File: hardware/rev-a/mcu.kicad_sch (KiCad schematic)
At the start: 6 parts, among them J1 Conn_01x05, SW1 SW_Push, U3 MDBT42Q-512K

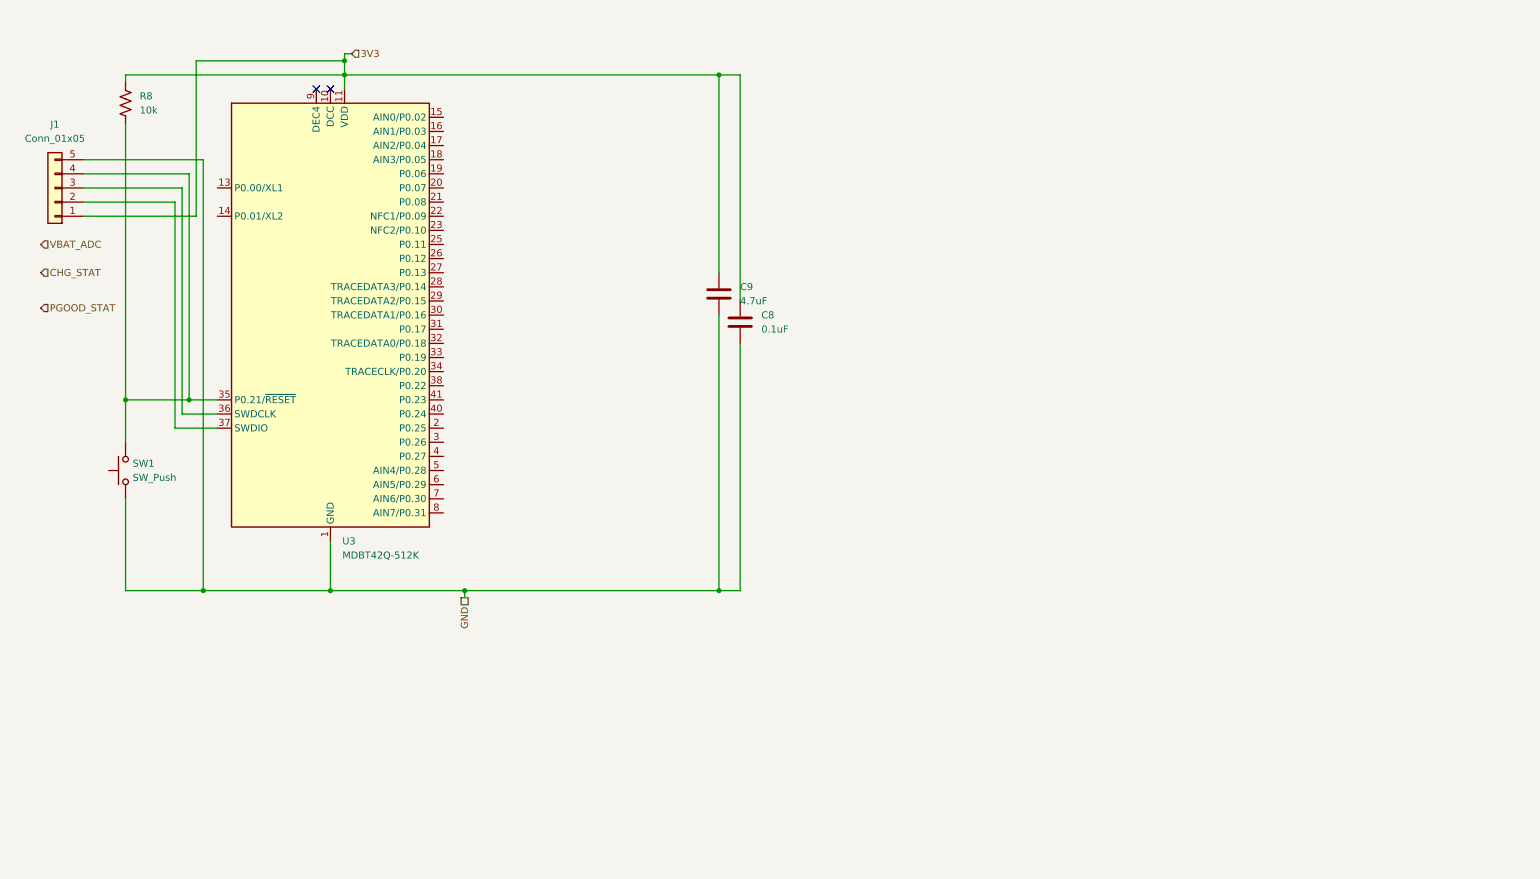
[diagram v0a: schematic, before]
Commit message: finalize MCU sheet and add haptic feedback sheet
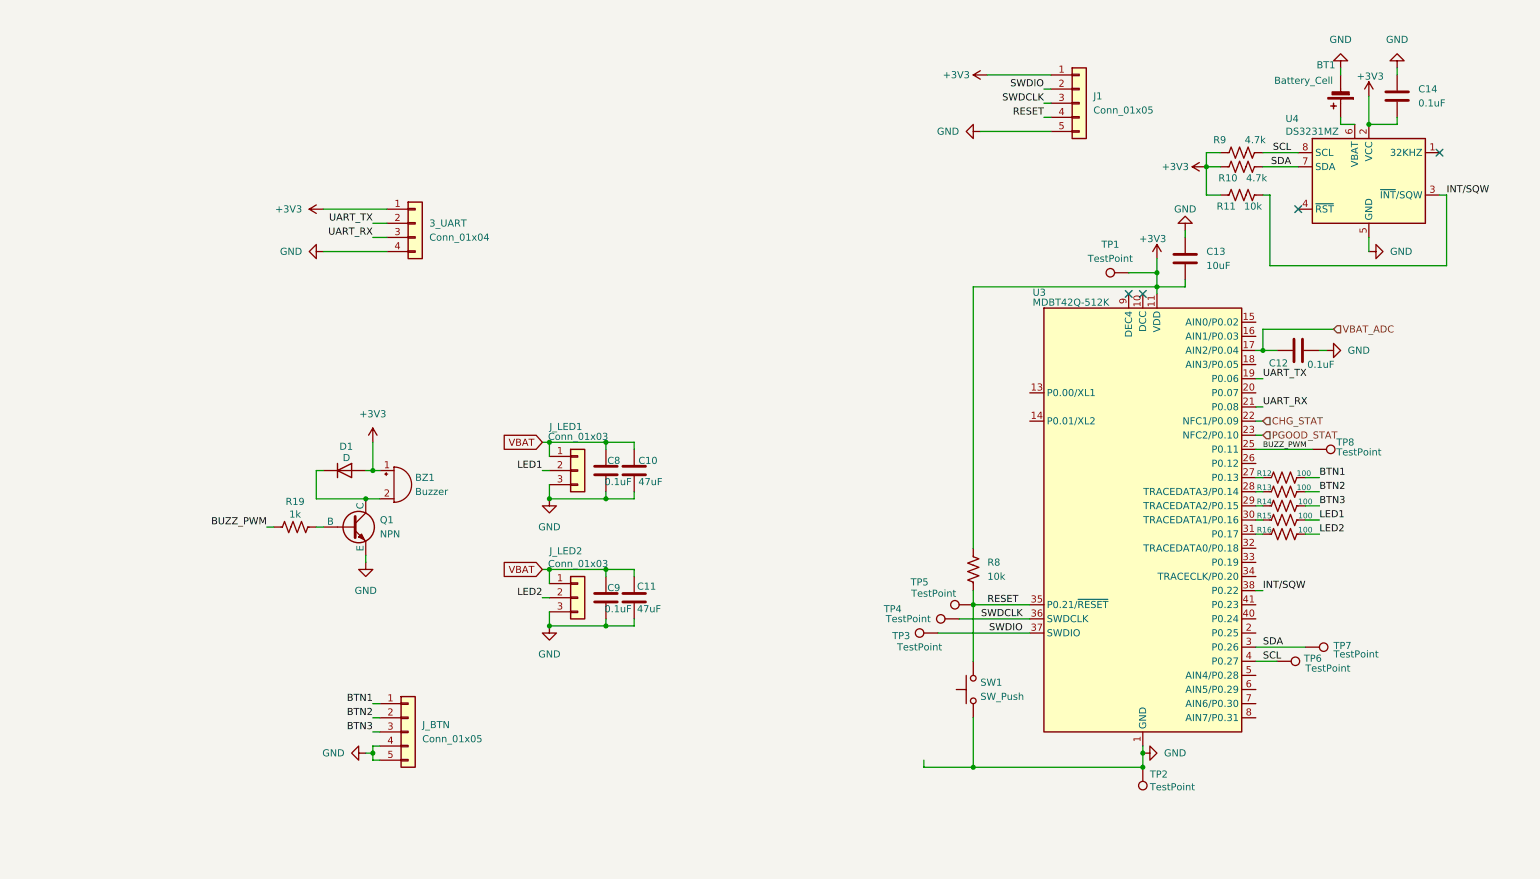
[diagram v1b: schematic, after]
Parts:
- added 3_UART: Conn_01x04, symbol Connector_Generic:Conn_01x04
- added BT1: Battery_Cell, symbol Device:Battery_Cell
- added BZ1: Buzzer, symbol Device:Buzzer
- added C10, C11: 47uF, symbol Device:C
- added C12, C14: 0.1uF, symbol Device:C
- added C13: 10uF, symbol Device:C
- added D1: D, symbol Device:D
- added J_BTN: Conn_01x05, symbol Connector_Generic:Conn_01x05
- added J_LED1, J_LED2: Conn_01x03, symbol Connector_Generic:Conn_01x03
- added Q1: NPN, symbol Simulation_SPICE:NPN
- added R10, R9: 4.7k, symbol Device:R_US
- added R11: 10k, symbol Device:R_US
- added R12, R13, R14, R15, R16: 100, symbol Device:R_US
- added R19: 1k, symbol Device:R_US
- added TP1, TP2, TP3, TP4, TP5, TP6, TP7, TP8: TestPoint, symbol Connector:TestPoint
- added U4: DS3231MZ, Package_SO:SOIC-8_3.9x4.9mm_P1.27mm, symbol Timer_RTC:DS3231MZ
- C9: value 4.7uF -> 0.1uF
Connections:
- net CHG_STAT: now also U3.22 (NFC1/P0.09)
- net GND: now also 3_UART.4 (Pin_4), BT1.2 (-), C10.2, C11.2, C12.2, C13.1, C14.1, J_BTN.4 (Pin_4), J_BTN.5 (Pin_5), J_LED1.3 (Pin_3), J_LED2.3 (Pin_3), Q1.3 (E), TP2.1, U4.5 (GND)
- net PGOOD_STAT: now also U3.23 (NFC2/P0.10)
- net VBAT_ADC: now also U3.17 (AIN2/P0.04), C12.1
- net UART_TX: now reaches U3.19 (P0.06)
- net UART_TX: now also 3_UART.2 (Pin_2)
- net UART_RX: now reaches U3.21 (P0.08)
- net UART_RX: now also 3_UART.3 (Pin_3)
- net BUZZ_PWM: now reaches U3.25 (P0.11)
- net BUZZ_PWM: now also R19.1, TP8.1
- net at U3.27 (P0.13): now also R12.1
- net at U3.28 (TRACEDATA3/P0.14): now also R13.1
- net at U3.29 (TRACEDATA2/P0.15): now also R14.1
- net SDA: now reaches U3.3 (P0.26)
- net SDA: now also R10.2, TP7.1, U4.7 (SDA)
- net at U3.30 (TRACEDATA1/P0.16): now also R15.2
- net at U3.31 (P0.17): now also R16.2
- net RESET: now reaches J1.4 (Pin_4), R8.2, SW1.2, U3.35 (P0.21/~{RESET})
- net RESET: now also TP5.1
- net SWDCLK: now reaches J1.3 (Pin_3), U3.36 (SWDCLK)
- net SWDCLK: now also TP4.1
- net SWDIO: now reaches J1.2 (Pin_2), U3.37 (SWDIO)
- net SWDIO: now also TP3.1
- net INT/SQW: now reaches U3.38 (P0.22)
- net INT/SQW: now also R11.2, U4.3 (~{INT}/SQW)
- net SCL: now reaches U3.4 (P0.27)
- net SCL: now also R9.2, TP6.1, U4.8 (SCL)
- net 3V3 renamed +3V3
- net +3V3: now also 3_UART.1 (Pin_1), BZ1.1 (+), C13.2, C14.2, D1.2 (A), R10.1, R11.1, R9.1, TP1.1, U4.2 (VCC); no longer C8.1, C9.1
- new net: BZ1.2 (-), D1.1 (K), Q1.1 (C)
- new net: Q1.2 (B), R19.2
- new net: BT1.1 (+), U4.6 (VBAT)
- new net BTN1: J_BTN.1 (Pin_1), R12.2
- new net BTN2: J_BTN.2 (Pin_2), R13.2
- new net BTN3: J_BTN.3 (Pin_3), R14.2
- new net LED1: J_LED1.2 (Pin_2), R15.1
- new net LED2: J_LED2.2 (Pin_2), R16.1
- new net VBAT: C10.1, C11.1, C8.1, C9.1, J_LED1.1 (Pin_1), J_LED2.1 (Pin_1)
- no-connect marks 2 -> 4
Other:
- title: (none) -> Microcontroller 
- moved on the sheet: J1, R8, SW1, U3

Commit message: Annotate schematic hierarchy and fix LED routing
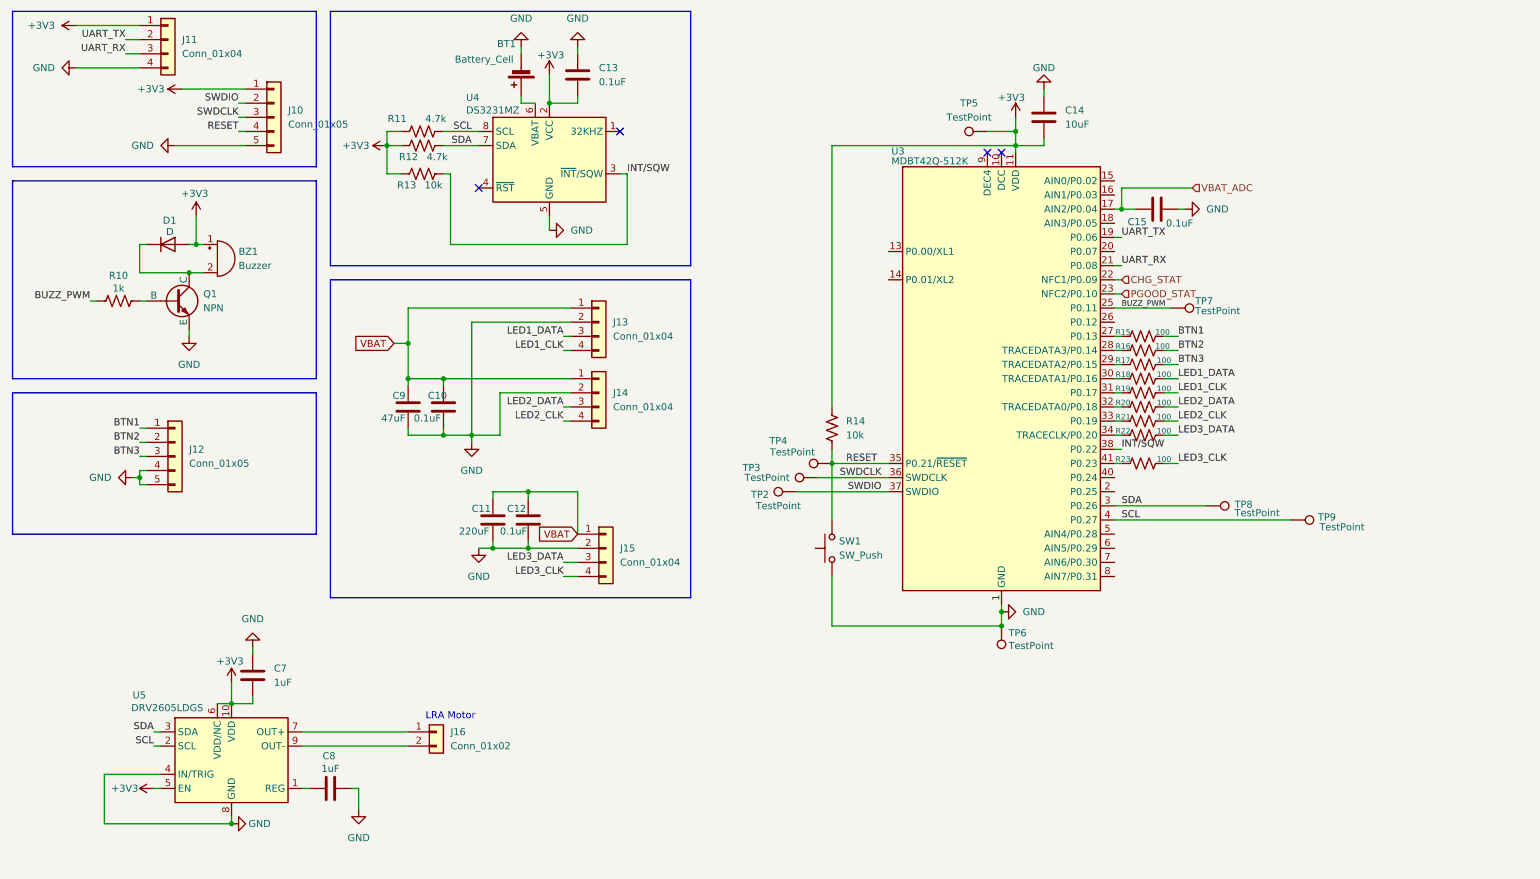
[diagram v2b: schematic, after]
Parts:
- removed J_LED1, J_LED2: Conn_01x03, symbol Connector_Generic:Conn_01x03
- added C12: 0.1uF, symbol Device:C
- added C7: 1uF, symbol Device:C
- added J13, J14, J15: Conn_01x04, symbol Connector_Generic:Conn_01x04
- added J16: Conn_01x02, symbol Connector_Generic:Conn_01x02
- added R20, R21, R22, R23: 100, symbol Device:R_US
- added U5: DRV2605LDGS, Package_SO:VSSOP-10_3x3mm_P0.5mm, symbol Driver_Haptic:DRV2605LDGS
- C10: value 47uF -> 0.1uF
- C11: value 47uF -> 220uF
- C8: value 0.1uF -> 1uF
- C9: value 0.1uF -> 47uF
- renumbered C14 to C13, C13 to C14, C12 to C15, J1 to J10, 3_UART to J11, J_BTN to J12, R19 to R10, R9 to R11, R10 to R12, R11 to R13, R8 to R14, R12 to R15, R13 to R16, R14 to R17, R15 to R18, R16 to R19, TP3 to TP2, TP4 to TP3, TP5 to TP4, TP1 to TP5, TP2 to TP6, TP8 to TP7, TP7 to TP8, TP6 to TP9
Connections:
- net +3V3: now also C7.2, U5.10 (VDD), U5.5 (EN), U5.6 (VDD/NC)
- net GND: now also C12.2, C7.1, J13.2 (Pin_2), J14.2 (Pin_2), J15.2 (Pin_2), U5.4 (IN/TRIG), U5.8 (GND)
- net SCL: now also U5.2 (SCL)
- net SDA: now also U5.3 (SDA)
- net VBAT: now also C12.1, J13.1 (Pin_1), J14.1 (Pin_1), J15.1 (Pin_1); no longer C8.1
- net at U3.32 (TRACEDATA0/P0.18): now also R20.2
- net at U3.33 (P0.19): now also R21.2
- net at U3.34 (TRACECLK/P0.20): now also R22.2
- net at U3.41 (P0.23): now also R23.2
- net LED1 renamed LED1_DATA
- net LED1_DATA: now also J13.3 (Pin_3)
- net LED2 renamed LED1_CLK
- net LED1_CLK: now also J13.4 (Pin_4)
- new net: C8.1, U5.1 (REG)
- new net: J16.1 (Pin_1), U5.7 (OUT+)
- new net: J16.2 (Pin_2), U5.9 (OUT-)
- new net LED2_CLK: J14.4 (Pin_4), R21.1
- new net LED2_DATA: J14.3 (Pin_3), R20.1
- new net LED3_CLK: J15.4 (Pin_4), R23.1
- new net LED3_DATA: J15.3 (Pin_3), R22.1
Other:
- note added: "LRA Motor"
- title: Microcontroller  -> Microcontroller & Connectors
- moved on the sheet: BT1, BZ1, C13, C14, C15, D1, J10, J11, J12, Q1, R10, R11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

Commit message: rev: schematic revision B
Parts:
- BT1: footprint (none) -> Battery:BatteryHolder_Keystone_103_1x20mm
- BZ1: footprint (none) -> TerminalBlock:TerminalBlock_MaiXu_MX126-5.0-02P_1x02_P5.00mm
- C10, C12, C13, C14, C15, C7, C8, C9: footprint (none) -> Capacitor_SMD:C_0603_1608Metric
- C11: footprint (none) -> Capacitor_SMD:CP_Elec_5x5.4
- D1: footprint (none) -> Diode_SMD:D_SOD-123
- J11: footprint (none) -> Connector_PinHeader_2.54mm:PinHeader_1x04_P2.54mm_Vertical
- J12: footprint (none) -> Connector_JST:JST_PH_B5B-PH-K_1x05_P2.00mm_Vertical
- J13, J14, J15: footprint (none) -> Connector_JST:JST_PH_B4B-PH-K_1x04_P2.00mm_Vertical
- J16: footprint (none) -> Connector_JST:JST_PH_B2B-PH-K_1x02_P2.00mm_Vertical
- Q1: footprint (none) -> Package_TO_SOT_SMD:SOT-23
- R10, R11, R12, R13, R14, R15, R16, R17, R18, R19, R20, R21, R22, R23: footprint (none) -> Resistor_SMD:R_0603_1608Metric
- SW1: footprint (none) -> Button_Switch_SMD:SW_SPST_TL3342
- TP2, TP3, TP4, TP5, TP6, TP7, TP8, TP9: footprint (none) -> TestPoint:TestPoint_Pad_D1.0mm
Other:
- moved on the sheet: BT1

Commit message: intialize PCB layout document
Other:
- note added: "2 Individual LEDs Headers"
- note added: "Buttons Header (3 buttons tied to same ground)"
- note added: "LED Strip Header"
- note added: "MCU Module"
- note added: "Motor Driver"
- note added: "NPN + Buzzer"
- note added: "RTC + Battery Cell"
- note added: "SWD Header"
- note added: "UART Header"
- moved on the sheet: R14
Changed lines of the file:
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@@
 		(comment 2 "Assigned footprints")
 	)
+	(text "LED Strip Header"
+		(exclude_from_sim no)
+		(at 84.582 112.522 0)
+		(effects
+			(font
+				(size 1.27 1.27)
+			)
+		)
+	)
+	(text "MCU Module"
+		(exclude_from_sim no)
+		(at 213.36 38.608 0)
+		(effects
+			(font
+				(size 1.27 1.27)
+			)
+		)
+	)
+	(text "RTC + Battery Cell"
+		(exclude_from_sim no)
+		(at 81.026 56.134 0)
+		(effects
+			(font
+				(size 1.27 1.27)
+			)
+		)
+	)
 	(text "LRA Motor"
 		(exclude_from_sim no)
@@
 		)
 	)
+	(text "Motor Driver"
+		(exclude_from_sim no)
+		(at 62.23 138.43 0)
+		(effects
+			(font
+				(size 1.27 1.27)
+			)
+		)
+	)
+	(text "UART Header"
+		(exclude_from_sim no)
+		(at 49.276 14.986 0)
+		(effects
+			(font
+				(size 1.27 1.27)
+			)
+		)
+	)
+	(text "SWD Header"
+		(exclude_from_sim no)
+		(at 48.26 39.37 0)
+		(effects
+			(font
+				(size 1.27 1.27)
+			)
+		)
+	)
+	(text "Buttons Header (3 buttons tied to same ground)"
+		(exclude_from_sim no)
+		(at 40.64 102.616 0)
+		(effects
+			(font
+				(size 1.27 1.27)
+			)
+		)
+	)
+	(text "NPN + Buzzer"
+		(exclude_from_sim no)
+		(at 21.336 76.454 0)
+		(effects
+			(font
+				(size 1.27 1.27)
+			)
+		)
+	)
+	(text "2 Individual LEDs Headers"
+		(exclude_from_sim no)
+		(at 119.38 90.424 0)
+		(effects
+			(font
+				(size 1.27 1.27)
+			)
+		)
+	)
 	(junction
 		(at 52.07 137.16)
@@
 	(wire
 		(pts
-			(xy 160.02 36.83) (xy 160.02 83.82)
+			(xy 160.02 36.83) (xy 160.02 72.39)
 		)
 		(stroke
@@
 	(wire
 		(pts
-			(xy 160.02 91.44) (xy 160.02 93.98)
+			(xy 160.02 80.01) (xy 160.02 93.98)
 		)
 		(stroke
@@
 		)
 	)
+	(wire
+		(pts
+			(xy 201.93 120.65) (xy 190.5 120.65)
+		)
+		(stroke
+			(width 0)
+			(type default)
+		)
+	)
 	(bus
 		(pts
@@
 	(symbol
 		(lib_id "power:GND")
-		(at 190.5 120.65 90)
+		(at 201.93 120.65 0)
 		(unit 1)
 		(exclude_from_sim no)
@@
 		(fields_autoplaced yes)
 		(property "Reference" "#PWR037"
-			(at 196.85 120.65 0)
+			(at 201.93 127 0)
 			(effects
 				(font
@@
 		)
 		(property "Value" "GND"
-			(at 194.31 120.6499 90)
+			(at 204.47 121.9199 0)
 			(effects
 				(font
 					(size 1.27 1.27)
 				)
-				(justify right)
+				(justify left)
 			)
 		)
 		(property "Footprint" ""
-			(at 190.5 120.65 0)
+			(at 201.93 120.65 0)
 			(effects
 				(font
@@
 		)
 		(property "Datasheet" ""
-			(at 190.5 120.65 0)
+			(at 201.93 120.65 0)
 			(effects
 				(font
@@
 		)
 		(property "Description" "Power symbol creates a global label with name \"GND\" , ground"
-			(at 190.5 120.65 0)
+			(at 201.93 120.65 0)
 			(effects
 				(font
@@
 	(symbol
 		(lib_id "Device:R_US")
-		(at 160.02 87.63 0)
+		(at 160.02 76.2 0)
 		(unit 1)
 		(exclude_from_sim no)
@@
 		(fields_autoplaced yes)
 		(property "Reference" "R14"
-			(at 162.56 86.3599 0)
+			(at 162.56 74.9299 0)
 			(effects
 				(font
@@
 		)
 		(property "Value" "10k"
-			(at 162.56 88.8999 0)
+			(at 162.56 77.4699 0)
 			(effects
 				(font
@@
 		)
 		(property "Footprint" "Resistor_SMD:R_0603_1608Metric"
-			(at 161.036 87.884 90)
+			(at 161.036 76.454 90)
 			(effects
 				(font
@@
 		)
 		(property "Datasheet" "~"
-			(at 160.02 87.63 0)
+			(at 160.02 76.2 0)
 			(effects
 				(font
@@
 		)
 		(property "Description" "Resistor, US symbol"
-			(at 160.02 87.63 0)
+			(at 160.02 76.2 0)
 			(effects
 				(font
